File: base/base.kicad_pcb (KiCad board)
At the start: 2 copper layers, 100 x 100 mm, 25 parts, among them J1 FTDI, J2 Barrel_Jack, J3 CONN_01X40, SW1 SW_Push, U1 Z80CPU, U2 27C256, U3 7404, U4 55257, U5 7432, U6 16550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

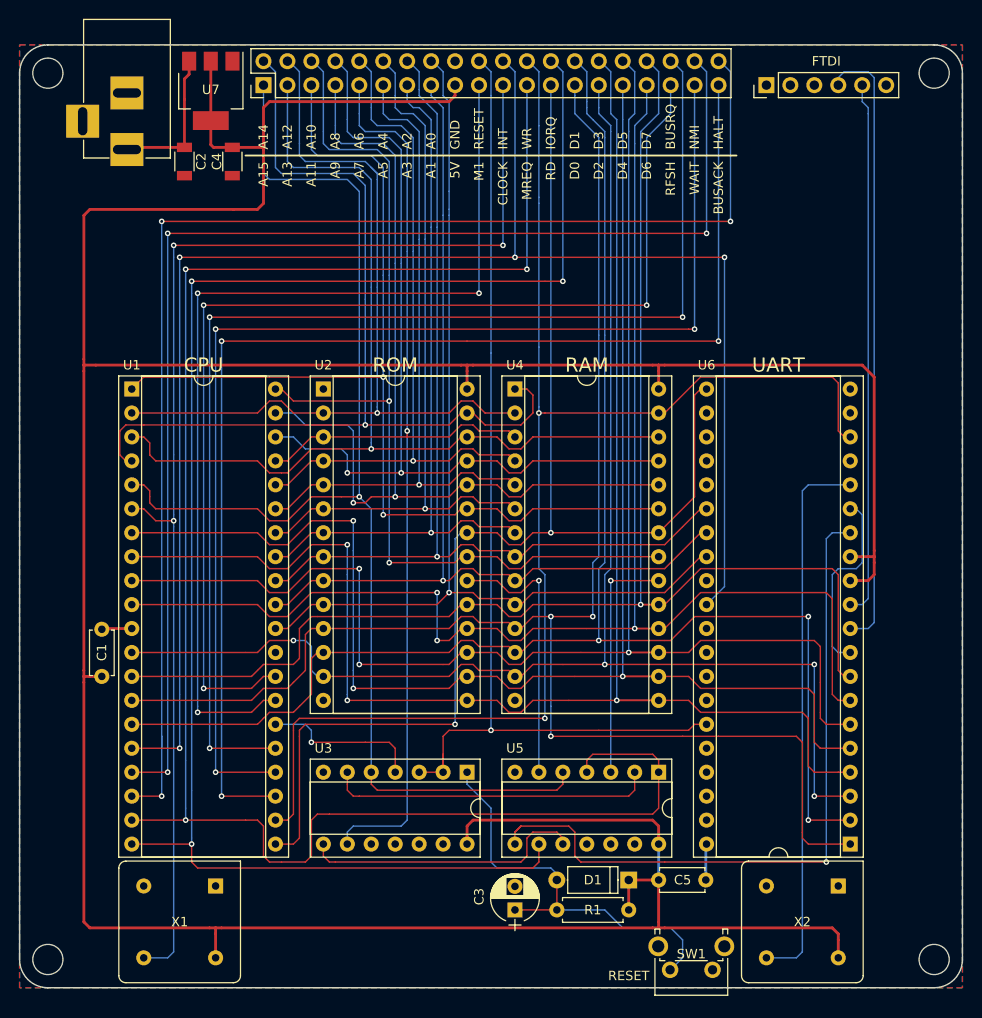
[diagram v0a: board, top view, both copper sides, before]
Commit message: Fixed decoupling caps
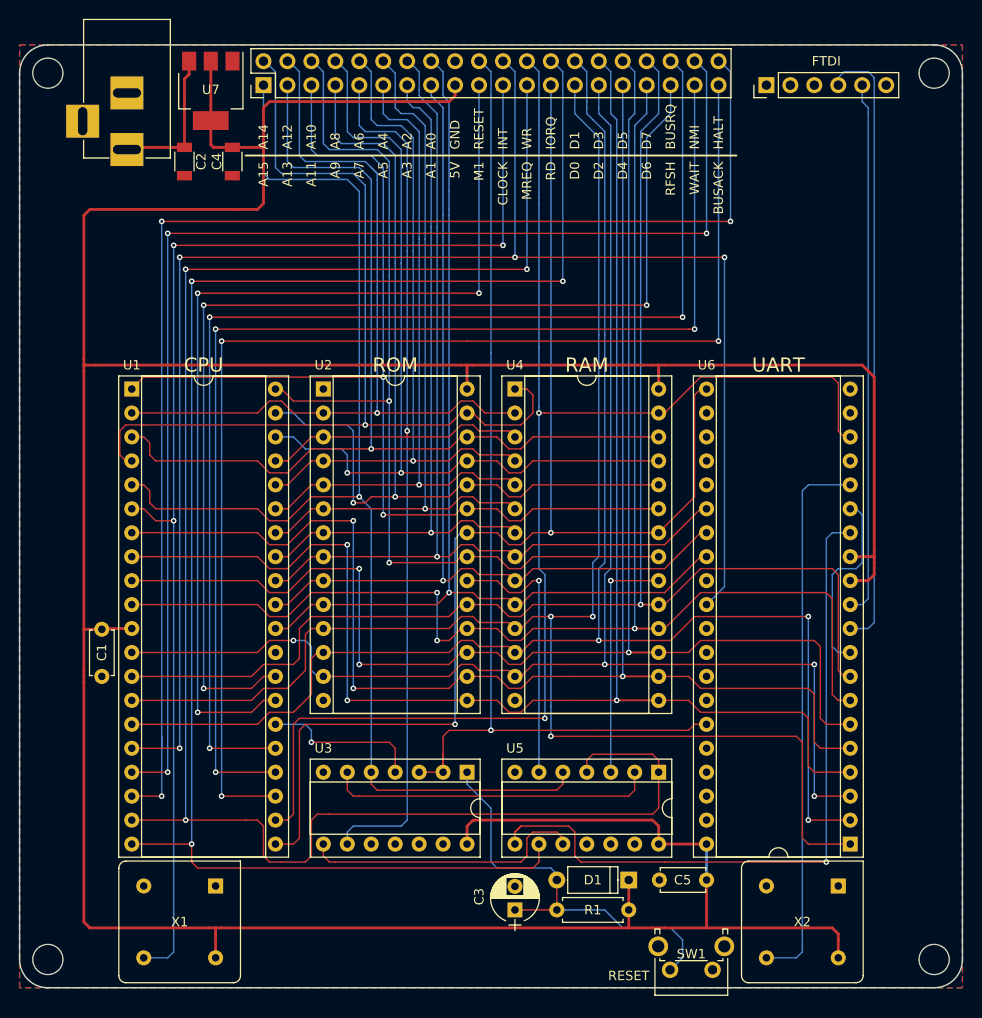
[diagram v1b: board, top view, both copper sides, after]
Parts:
- C5: value C_Small -> .1 uF
- moved C5 5.08 mm to (127.0, 148.6), turned to 180 degrees
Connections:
- C1 pad 1: +5V -> GND
- C1 pad 2: Net-(C1-Pad2) -> +5V
- C5 pad 2: Net-(C5-Pad2) -> GND
- U1 pad 11: Net-(C1-Pad2) -> +5V
- U6 pad 40: Net-(C5-Pad2) -> +5V
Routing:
- net +5V: track 385.9 -> 393.4 mm
- net Net-(C5-Pad2): track 3.84 -> 0.00 mm
- net Net-(C1-Pad2): track 3.55 -> 0.00 mm

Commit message: Clean up schematic and added more decoupling
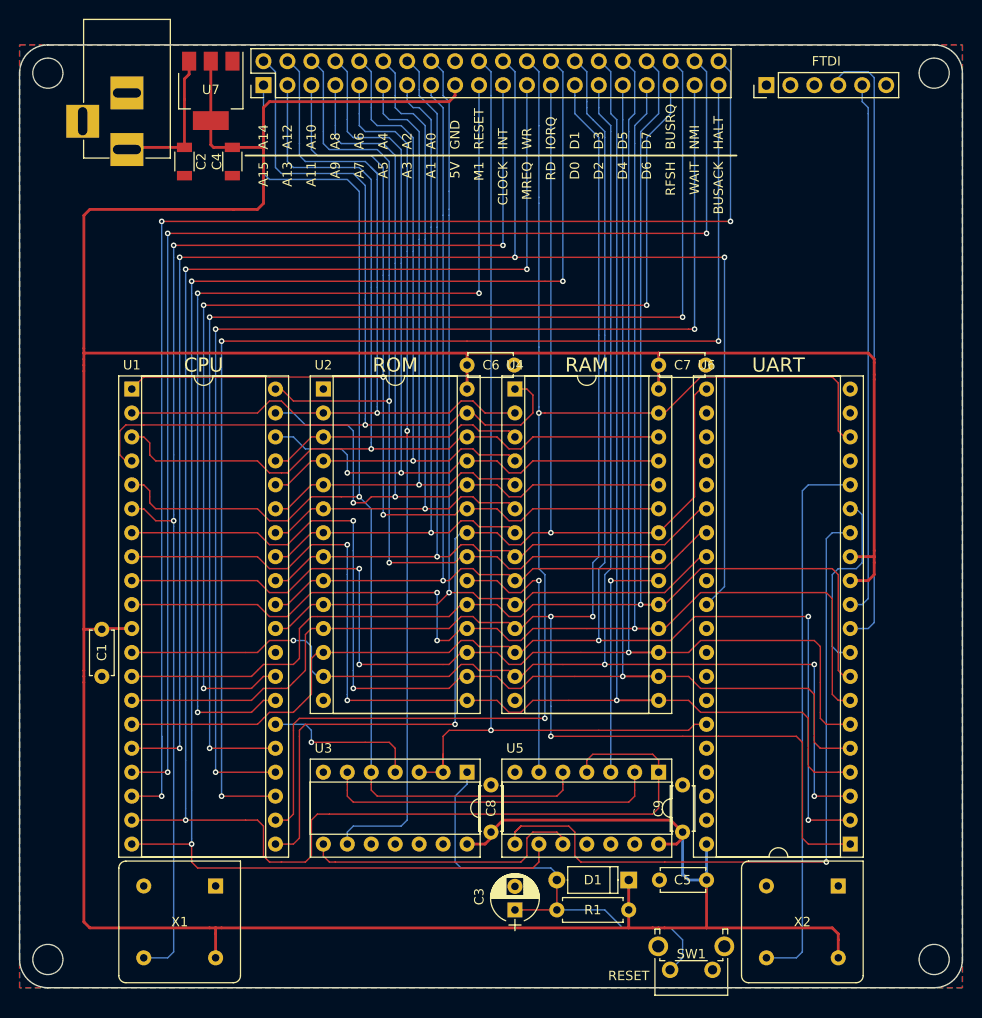
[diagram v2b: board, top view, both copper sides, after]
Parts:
- added C6: .1 uF, Capacitors_THT:C_Disc_D4.7mm_W2.5mm_P5.00mm, F.Cu at (101.6, 94.0)
- added C7: .1 uF, Capacitors_THT:C_Disc_D4.7mm_W2.5mm_P5.00mm, F.Cu at (121.9, 94.0)
- added C8: .1 uF, Capacitors_THT:C_Disc_D4.7mm_W2.5mm_P5.00mm, F.Cu at (104.1, 143.5)
- added C9: .1 uF, Capacitors_THT:C_Disc_D4.7mm_W2.5mm_P5.00mm, F.Cu at (124.5, 143.5)
- C1: value 1 uF -> .1 uF
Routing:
- net +5V: track 393.4 -> 403.4 mm
- net Net-(C3-Pad1): track 45.4 -> 48.7 mm
- net Net-(U3-Pad6): track 34.8 -> 36.1 mm
- net /A15: track 134.6 -> 135.9 mm

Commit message: Cleaned up layout
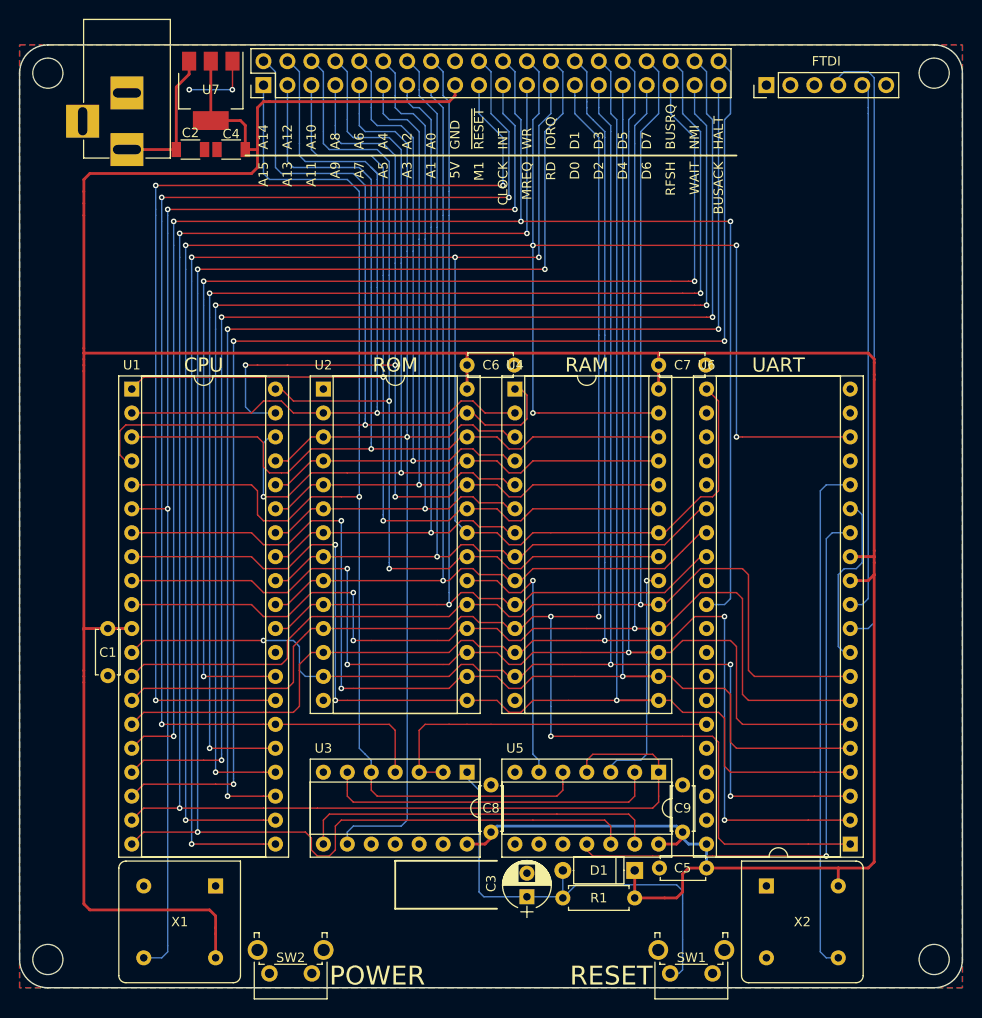
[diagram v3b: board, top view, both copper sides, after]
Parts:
- added SW2: POWER, Buttons_Switches_THT:SW_Tactile_SPST_Angled_PTS645Vx31-2LFS, F.Cu at (85.1, 158.5)
- SW1: value SW_Push -> RESET
- moved X2 7.62 mm to (133.3, 149.2), turned to 270 degrees
- moved C1 5.12 mm to (63.5, 121.9), turned to 270 degrees
- moved C3 1.89 mm to (108.0, 150.4)
- moved C2 1.42 mm to (72.3, 71.1), turned to 0 degrees
- moved R1 1.42 mm to (119.4, 150.5)
- moved C4 1.28 mm to (76.6, 71.1), turned to 180 degrees
- moved C5 1.27 mm to (127.0, 147.3)
- moved D1 1.20 mm to (119.4, 147.6)
- moved SW1 0.39 mm to (127.6, 158.5)
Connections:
- C1 pad 1: GND -> +5V
- C1 pad 2: +5V -> GND
- J3 pad 20: RESET -> ~RESET~
- U5 pad 10: Net-(U3-Pad8) -> Net-(U5-Pad10)
- U5 pad 11: (no net) -> UART_CE
- U5 pad 12: (no net) -> IORQ
- U5 pad 13: (no net) -> Net-(U3-Pad8)
- U5 pad 8: UART_CE -> Net-(U5-Pad8)
- U5 pad 9: IORQ -> Net-(U5-Pad9)
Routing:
- net ~RESET~: track 17.0 -> 138.2 mm, vias 1 -> 3
- net RESET: track 108.9 -> 38.4 mm, vias 1 -> 0
- net WR: track 149.4 -> 215.4 mm, vias 2 -> 6
- net RD: track 141.0 -> 201.4 mm, vias 2 -> 4
- net +5V: track 403.4 -> 380.4 mm
- net UART_CE: track 75.6 -> 62.8 mm
- net M1: track 105.8 -> 116.5 mm
- net MREQ: track 192.8 -> 184.0 mm
- net Net-(U3-Pad8): track 30.9 -> 39.3 mm
- net GND: track 0.00 -> 8.24 mm, vias 0 -> 2
- net IORQ: track 170.5 -> 178.4 mm
- net /A8: track 93.8 -> 100.7 mm
- net INT: track 174.8 -> 180.1 mm
- net Net-(U6-Pad16): track 58.9 -> 54.5 mm
- net RFSH: track 120.8 -> 124.1 mm
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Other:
- board text added: "POWER"
- board text added: "Rev. 2"
- board text added: "~RESET~"
- board text removed: "Rev. 1"

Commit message: Added pullups to busrq and int pins
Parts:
- added R2: 10k, Resistors_THT:R_Axial_DIN0207_L6.3mm_D2.5mm_P7.62mm_Horizontal, F.Cu at (62.9, 134.6)
- added R3: 10k, Resistors_THT:R_Axial_DIN0207_L6.3mm_D2.5mm_P7.62mm_Horizontal, F.Cu at (91.4, 134.0)
- moved C1 0.63 mm to (62.9, 121.9)
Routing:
- net +5V: track 380.4 -> 394.2 mm
- net BUSRQ: track 133.5 -> 143.9 mm
- net INT: track 180.1 -> 183.3 mm
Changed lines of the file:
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@@
     (thickness 1.6)
     (drawings 61)
-    (tracks 1184)
+    (tracks 1194)
     (zones 0)
-    (modules 30)
+    (modules 32)
     (nets 76)
   )
@@
   )
   (module Capacitors_THT:C_Disc_D4.7mm_W2.5mm_P5.00mm (layer F.Cu)
-    (at 63.5 121.92 270)
+    (at 62.865 121.92 270)
     (descr "C, Disc series, Radial, pin pitch=5.00mm, , diameter*width=4.7*2.5mm^2, Capacitor, http://www.vishay.com/docs/45233/krseries.pdf")
     (tags "C Disc series Radial pin pitch 5.00mm  diameter 4.7mm width 2.5mm Capacitor")
@@
       (at (xyz 0 0 0))
       (scale (xyz 1 1 1))
+      (rotate (xyz 0 0 0))
+    )
+  )
+  (module Resistors_THT:R_Axial_DIN0207_L6.3mm_D2.5mm_P7.62mm_Horizontal (layer F.Cu)
+    (at 62.865 134.62 270)
+    (descr "Resistor, Axial_DIN0207 series, Axial, Horizontal, pin pitch=7.62mm, 0.25W = 1/4W, length*diameter=6.3*2.5mm^2, http://cdn-reichelt.de/documents/datenblatt/B400/1_4W%23YAG.pdf")
+    (tags "Resistor Axial_DIN0207 series Axial Horizontal pin pitch 7.62mm 0.25W = 1/4W length 6.3mm diameter 2.5mm")
+    (fp_text reference R2 (at 3.81 0) (layer F.SilkS)
+      (effects (font (size 1 1) (thickness 0.15)))
+    )
+    (fp_text value 10k (at 3.81 2.31 270) (layer F.Fab)
+      (effects (font (size 1 1) (thickness 0.15)))
+    )
+    (fp_line (start 8.7 -1.6) (end -1.05 -1.6) (layer F.CrtYd) (width 0.05))
+    (fp_line (start 8.7 1.6) (end 8.7 -1.6) (layer F.CrtYd) (width 0.05))
+    (fp_line (start -1.05 1.6) (end 8.7 1.6) (layer F.CrtYd) (width 0.05))
+    (fp_line (start -1.05 -1.6) (end -1.05 1.6) (layer F.CrtYd) (width 0.05))
+    (fp_line (start 7.02 1.31) (end 7.02 0.98) (layer F.SilkS) (width 0.12))
+    (fp_line (start 0.6 1.31) (end 7.02 1.31) (layer F.SilkS) (width 0.12))
+    (fp_line (start 0.6 0.98) (end 0.6 1.31) (layer F.SilkS) (width 0.12))
+    (fp_line (start 7.02 -1.31) (end 7.02 -0.98) (layer F.SilkS) (width 0.12))
+    (fp_line (start 0.6 -1.31) (end 7.02 -1.31) (layer F.SilkS) (width 0.12))
+    (fp_line (start 0.6 -0.98) (end 0.6 -1.31) (layer F.SilkS) (width 0.12))
+    (fp_line (start 7.62 0) (end 6.96 0) (layer F.Fab) (width 0.1))
+    (fp_line (start 0 0) (end 0.66 0) (layer F.Fab) (width 0.1))
+    (fp_line (start 6.96 -1.25) (end 0.66 -1.25) (layer F.Fab) (width 0.1))
+    (fp_line (start 6.96 1.25) (end 6.96 -1.25) (layer F.Fab) (width 0.1))
+    (fp_line (start 0.66 1.25) (end 6.96 1.25) (layer F.Fab) (width 0.1))
+    (fp_line (start 0.66 -1.25) (end 0.66 1.25) (layer F.Fab) (width 0.1))
+    (pad 2 thru_hole oval (at 7.62 0 270) (size 1.6 1.6) (drill 0.8) (layers *.Cu *.Mask)
+      (net 15 +5V))
+    (pad 1 thru_hole circle (at 0 0 270) (size 1.6 1.6) (drill 0.8) (layers *.Cu *.Mask)
+      (net 60 INT))
+    (model ${KISYS3DMOD}/Resistors_THT.3dshapes/R_Axial_DIN0207_L6.3mm_D2.5mm_P7.62mm_Horizontal.wrl
+      (at (xyz 0 0 0))
+      (scale (xyz 0.393701 0.393701 0.393701))
+      (rotate (xyz 0 0 0))
+    )
+  )
+  (module Resistors_THT:R_Axial_DIN0207_L6.3mm_D2.5mm_P7.62mm_Horizontal (layer F.Cu)
+    (at 91.44 133.985)
+    (descr "Resistor, Axial_DIN0207 series, Axial, Horizontal, pin pitch=7.62mm, 0.25W = 1/4W, length*diameter=6.3*2.5mm^2, http://cdn-reichelt.de/documents/datenblatt/B400/1_4W%23YAG.pdf")
+    (tags "Resistor Axial_DIN0207 series Axial Horizontal pin pitch 7.62mm 0.25W = 1/4W length 6.3mm diameter 2.5mm")
+    (fp_text reference R3 (at 3.81 -2.31) (layer F.SilkS)
+      (effects (font (size 1 1) (thickness 0.15)))
+    )
+    (fp_text value 10k (at 3.81 2.31) (layer F.Fab)
+      (effects (font (size 1 1) (thickness 0.15)))
+    )
+    (fp_line (start 0.66 -1.25) (end 0.66 1.25) (layer F.Fab) (width 0.1))
+    (fp_line (start 0.66 1.25) (end 6.96 1.25) (layer F.Fab) (width 0.1))
+    (fp_line (start 6.96 1.25) (end 6.96 -1.25) (layer F.Fab) (width 0.1))
+    (fp_line (start 6.96 -1.25) (end 0.66 -1.25) (layer F.Fab) (width 0.1))
+    (fp_line (start 0 0) (end 0.66 0) (layer F.Fab) (width 0.1))
+    (fp_line (start 7.62 0) (end 6.96 0) (layer F.Fab) (width 0.1))
+    (fp_line (start 0.6 -0.98) (end 0.6 -1.31) (layer F.SilkS) (width 0.12))
+    (fp_line (start 0.6 -1.31) (end 7.02 -1.31) (layer F.SilkS) (width 0.12))
+    (fp_line (start 7.02 -1.31) (end 7.02 -0.98) (layer F.SilkS) (width 0.12))
+    (fp_line (start 0.6 0.98) (end 0.6 1.31) (layer F.SilkS) (width 0.12))
+    (fp_line (start 0.6 1.31) (end 7.02 1.31) (layer F.SilkS) (width 0.12))
+    (fp_line (start 7.02 1.31) (end 7.02 0.98) (layer F.SilkS) (width 0.12))
+    (fp_line (start -1.05 -1.6) (end -1.05 1.6) (layer F.CrtYd) (width 0.05))
+    (fp_line (start -1.05 1.6) (end 8.7 1.6) (layer F.CrtYd) (width 0.05))
+    (fp_line (start 8.7 1.6) (end 8.7 -1.6) (layer F.CrtYd) (width 0.05))
+    (fp_line (start 8.7 -1.6) (end -1.05 -1.6) (layer F.CrtYd) (width 0.05))
+    (pad 1 thru_hole circle (at 0 0) (size 1.6 1.6) (drill 0.8) (layers *.Cu *.Mask)
+      (net 66 BUSRQ))
+    (pad 2 thru_hole oval (at 7.62 0) (size 1.6 1.6) (drill 0.8) (layers *.Cu *.Mask)
+      (net 15 +5V))
+    (model ${KISYS3DMOD}/Resistors_THT.3dshapes/R_Axial_DIN0207_L6.3mm_D2.5mm_P7.62mm_Horizontal.wrl
+      (at (xyz 0 0 0))
+      (scale (xyz 0.393701 0.393701 0.393701))
       (rotate (xyz 0 0 0))
     )
@@
   (segment (start 100.965 115.57) (end 102.235 115.57) (width 0.152) (layer F.Cu) (net 14))
   (segment (start 99.695 116.84) (end 100.965 115.57) (width 0.152) (layer F.Cu) (net 14))
+  (segment (start 99.06 133.985) (end 100.33 135.255) (width 0.3) (layer B.Cu) (net 15) (status 400000))
+  (segment (start 100.33 142.875) (end 101.6 144.145) (width 0.3) (layer B.Cu) (net 15) (status 800000))
+  (segment (start 100.33 135.255) (end 100.33 142.875) (width 0.3) (layer B.Cu) (net 15))
+  (segment (start 101.6 144.145) (end 101.6 144.78) (width 0.3) (layer B.Cu) (net 15) (status C00000))
+  (segment (start 62.865 142.24) (end 60.96 142.24) (width 0.3) (layer F.Cu) (net 15) (status 400000))
   (segment (start 125.095 147.32) (end 124.46 147.955) (width 0.3) (layer F.Cu) (net 15))
   (segment (start 123.825 150.495) (end 122.555 150.495) (width 0.3) (layer F.Cu) (net 15))
@@
   (segment (start 74.295 151.765) (end 61.595 151.765) (width 0.3) (layer F.Cu) (net 15))
   (segment (start 60.96 127) (end 60.96 127.635) (width 0.3) (layer F.Cu) (net 15))
-  (segment (start 60.96 127.635) (end 60.96 151.13) (width 0.3) (layer F.Cu) (net 15))
+  (segment (start 60.96 127.635) (end 60.96 142.24) (width 0.3) (layer F.Cu) (net 15))
+  (segment (start 60.96 142.24) (end 60.96 151.13) (width 0.3) (layer F.Cu) (net 15))
   (segment (start 60.96 126.365) (end 60.96 122) (width 0.3) (layer F.Cu) (net 15))
   (segment (start 60.96 126.365) (end 60.96 127) (width 0.3) (layer F.Cu) (net 15))
@@
   (segment (start 96.52 132.715) (end 97.155 132.08) (width 0.152) (layer F.Cu) (net 53))
   (segment (start 99.695 132.08) (end 101.6 132.08) (width 0.152) (layer F.Cu) (net 53))
+  (segment (start 62.865 134.62) (end 66.04 134.62) (width 0.152) (layer F.Cu) (net 60) (status C00000))
   (via (at 129.54 78.74) (size 0.6) (drill 0.3) (layers F.Cu B.Cu) (net 60))
   (segment (start 128.905 119.38) (end 129.54 118.745) (width 0.152) (layer B.Cu) (net 60))
@@
   (via (at 128.905 91.44) (size 0.6) (drill 0.3) (layers F.Cu B.Cu) (net 65))
   (segment (start 128.905 67.945) (end 128.905 91.44) (width 0.152) (layer B.Cu) (net 65))
+  (segment (start 81.28 134.62) (end 81.915 134.62) (width 0.152) (layer F.Cu) (net 66) (status C00000))
+  (segment (start 81.915 134.62) (end 82.55 133.985) (width 0.152) (layer F.Cu) (net 66) (status 400000))
+  (segment (start 82.55 133.985) (end 91.44 133.985) (width 0.152) (layer F.Cu) (net 66) (status 800000))
   (segment (start 125.73 68.58) (end 126.365 69.215) (width 0.152) (layer B.Cu) (net 66))
   (segment (start 126.365 86.36) (end 125.73 86.36) (width 0.152) (layer F.Cu) (net 66))

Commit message: Added pinout to silkscreen
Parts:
- moved REF*** 12.4 mm to (103.9, 85.5)
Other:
- board text added: "1A"
- board text added: "1B"
- board text added: "1Y"
- board text added: "2A"
- board text added: "2B"
- board text added: "2Y"
- board text added: "3A"
- board text added: "3B"
- board text added: "3Y"
- board text added: "4A"
- board text added: "4B"
- board text added: "4Y"
- board text added: "5A"
- board text added: "5Y"
- board text added: "6A"
- board text added: "6Y"
- board text added: "CLK"
- board text added: "CS0"
- board text added: "DDIS"
- board text added: "INTR"
- board text added: "MR"
- board text added: "RCLK"
- board text added: "SIN"
- board text added: "SOUT"
- board text added: "Vpp"
- board text added: "XIN"
- board text added: "XOUT"
- board text added: "~ADS~"
- board text added: "~BAUDOUT~"
- board text added: "~BUSACK~"
- board text added: "~BUSRQ~"
- board text added: "~CE~"
- board text added: "~CS1~"
- board text added: "~CS2~"
- board text added: "~CTS~"
- board text added: "~DCD~"
- board text added: "~DSR~"
- board text added: "~DTR~"
- board text added: "~HALT~"
- board text added: "~INT~"
- board text added: "~IORQ~"
- board text added: "~M1~"
- board text added: "~MREQ~"
- board text added: "~NMI~"
- board text added: "~OUT1~"
- board text added: "~OUT2~"
- board text added: "~RD~"
- board text added: "~RFSH~"
- board text added: "~RI"
- board text added: "~RTS~"
- board text added: "~RXRDY~"
- board text added: "~TXRDY~"
- board text added: "~WAIT~"
- board text added: "~WR~"
- board text removed: "BUSACK"
- board text removed: "BUSRQ"
- board text removed: "CLOCK"
- board text removed: "HALT"
- board text removed: "INT"
- board text removed: "IORQ"
- board text removed: "M1"
- board text removed: "MREQ"
- board text removed: "NMI"
- board text removed: "RFSH"
- board text removed: "WAIT"
